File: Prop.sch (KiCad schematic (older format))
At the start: 11 parts

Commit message: some changes
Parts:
- added J? (x3): 1984989, PHOENIX_1984989, symbol 1984989:1984989
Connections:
- net labels added: +5V, MISO_1, MISO_2, MISO_3
- net labels removed: MISO, PWR
- wire segments 72 -> 64
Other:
- note added: "From Load Cell"
- note added: "From Pressure Transducer"
- note added: "From Thermocouple Connector"
- note added: "To Thermocouple"
- note removed: "Microcontroller"
- note removed: "Thermocouple"
- moved on the sheet: J?, Resistor, Resistor?, U?

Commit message: smaller capacitors
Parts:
- removed C? (x3): 0.1uF, symbol pspice:CAP
- added C (x3): 0.1 uF, symbol Device:C
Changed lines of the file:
@@
 Alumel_Lead
 Connection ~ 7300 2300
-Wire Wire Line
-	7300 2200 7300 2300
-Wire Wire Line
-	7300 1400 7300 1700
-$Comp
-L pspice:CAP C?
-U 1 1 603AE0E4
-P 7300 1950
-F 0 "C?" H 7478 1996 50  0000 L CNN
-F 1 "0.1uF" H 7478 1905 50  0000 L CNN
-F 2 "" H 7300 1950 50  0001 C CNN
-F 3 "~" H 7300 1950 50  0001 C CNN
-	1    7300 1950
-	1    0    0    -1
-$EndComp
 $Comp
 L MAX6675ISA_:MAX6675ISA+ U?
@@
 Text Notes 2000 1900 0    50   ~ 0
 Pressure\nTransducer
-$Comp
-L pspice:CAP C?
-U 1 1 6041617D
-P 3150 1800
-F 0 "C?" H 3328 1846 50  0000 L CNN
-F 1 "0.1uF" H 3328 1755 50  0000 L CNN
-F 2 "" H 3150 1800 50  0001 C CNN
-F 3 "~" H 3150 1800 50  0001 C CNN
-	1    3150 1800
-	1    0    0    -1
-$EndComp
 Wire Wire Line
 	4800 1900 5050 1900
@@
 Wire Wire Line
 	1650 1550 1350 1550
-Wire Wire Line
-	2650 1350 3150 1350
 Wire Wire Line
 	2850 1550 2650 1550
@@
 	3150 1200 3150 1350
 Wire Wire Line
-	3150 2050 3150 2200
-Wire Wire Line
-	3150 2200 2850 2200
-Wire Wire Line
-	2850 2200 2850 1550
+	3150 1850 3150 2000
+Wire Wire Line
+	3150 2000 2850 2000
+Wire Wire Line
+	2850 2000 2850 1550
 $Comp
 L power:GND #PWR?
 U 1 1 603FE602
-P 3150 2350
-F 0 "#PWR?" H 3150 2100 50  0001 C CNN
-F 1 "GND" H 3155 2177 50  0000 C CNN
-F 2 "" H 3150 2350 50  0001 C CNN
-F 3 "" H 3150 2350 50  0001 C CNN
-	1    3150 2350
-	1    0    0    -1
-$EndComp
-Wire Wire Line
-	3150 2350 3150 2200
-Connection ~ 3150 2200
+P 3150 2150
+F 0 "#PWR?" H 3150 1900 50  0001 C CNN
+F 1 "GND" H 3155 1977 50  0000 C CNN
+F 2 "" H 3150 2150 50  0001 C CNN
+F 3 "" H 3150 2150 50  0001 C CNN
+	1    3150 2150
+	1    0    0    -1
+$EndComp
+Wire Wire Line
+	3150 2150 3150 2000
+Connection ~ 3150 2000
 Wire Wire Line
 	7300 1400 7300 1000
@@
 Wire Wire Line
 	4050 3850 4050 4750
-Wire Wire Line
-	2600 3400 2600 4050
 Connection ~ 1200 3400
 Wire Wire Line
@@
 	1    0    0    -1
 $EndComp
-$Comp
-L pspice:CAP C?
-U 1 1 60425283
-P 2600 4300
-F 0 "C?" H 2778 4346 50  0000 L CNN
-F 1 "0.1uF" H 2778 4255 50  0000 L CNN
-F 2 "" H 2600 4300 50  0001 C CNN
-F 3 "~" H 2600 4300 50  0001 C CNN
-	1    2600 4300
-	1    0    0    -1
-$EndComp
-Wire Wire Line
-	2600 4550 2600 4750
 $Comp
 L power:GND #PWR?
@@
 Text Notes 7450 3950 0    50   ~ 0
 From Pressure Transducer
+$Comp
+L Device:C C
+U 1 1 603C3DD0
+P 3150 1700
+F 0 "C" H 3265 1746 50  0000 L CNN
+F 1 "0.1 uF" H 3265 1655 50  0000 L CNN
+F 2 "" H 3188 1550 50  0001 C CNN
+F 3 "~" H 3150 1700 50  0001 C CNN
+	1    3150 1700
+	1    0    0    -1
+$EndComp
+Wire Wire Line
+	2650 1350 3150 1350
+$Comp
+L Device:C C
+U 1 1 603CA8F8
+P 7300 1950
+F 0 "C" H 7415 1996 50  0000 L CNN
+F 1 "0.1 uF" H 7415 1905 50  0000 L CNN
+F 2 "" H 7338 1800 50  0001 C CNN
+F 3 "~" H 7300 1950 50  0001 C CNN
+	1    7300 1950
+	1    0    0    -1
+$EndComp
+Wire Wire Line
+	7300 1400 7300 1800
+Wire Wire Line
+	7300 2100 7300 2300
+$Comp
+L Device:C C
+U 1 1 603D0090
+P 2600 4300
+F 0 "C" H 2715 4346 50  0000 L CNN
+F 1 "0.1 uF" H 2715 4255 50  0000 L CNN
+F 2 "" H 2638 4150 50  0001 C CNN
+F 3 "~" H 2600 4300 50  0001 C CNN
+	1    2600 4300
+	1    0    0    -1
+$EndComp
+Wire Wire Line
+	2600 3400 2600 4150
+Wire Wire Line
+	2600 4450 2600 4750
 $EndSCHEMATC

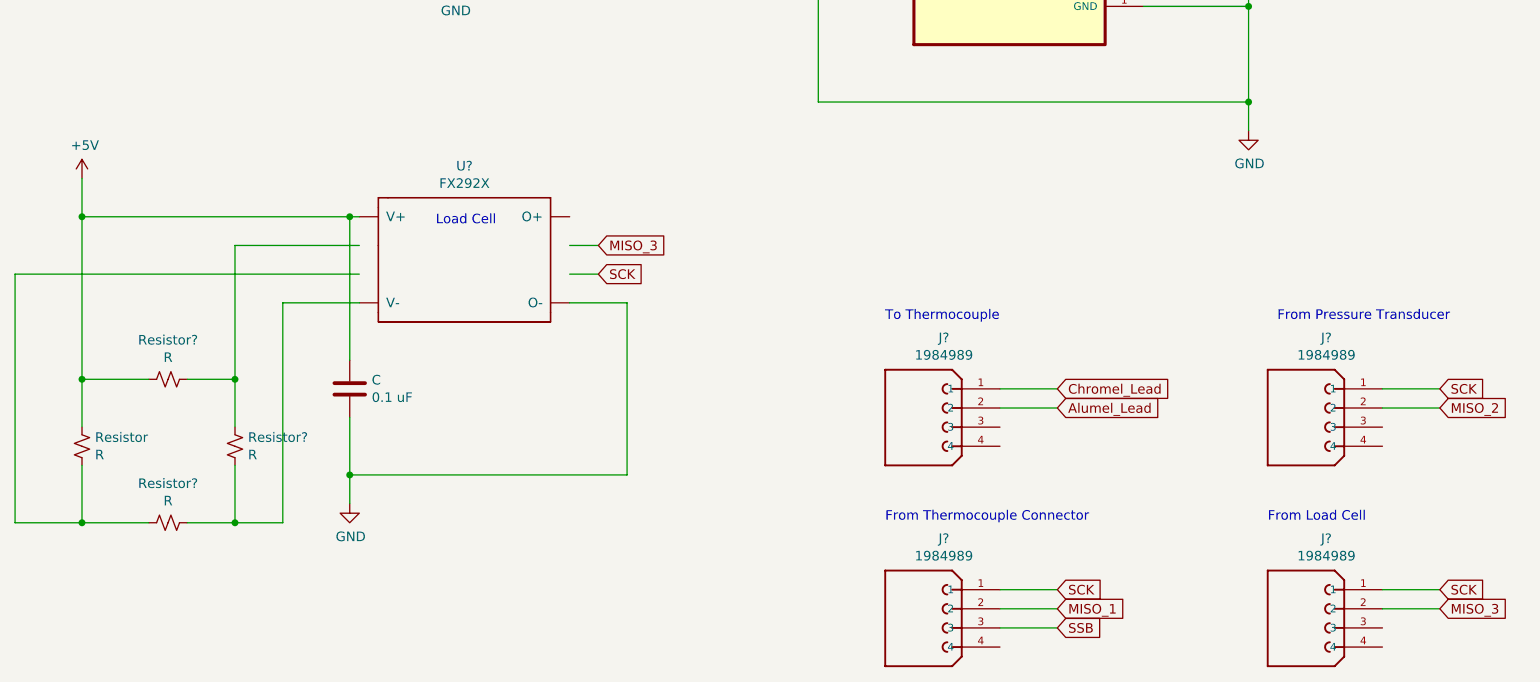
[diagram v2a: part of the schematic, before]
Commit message: changed load cell to have 4 pins
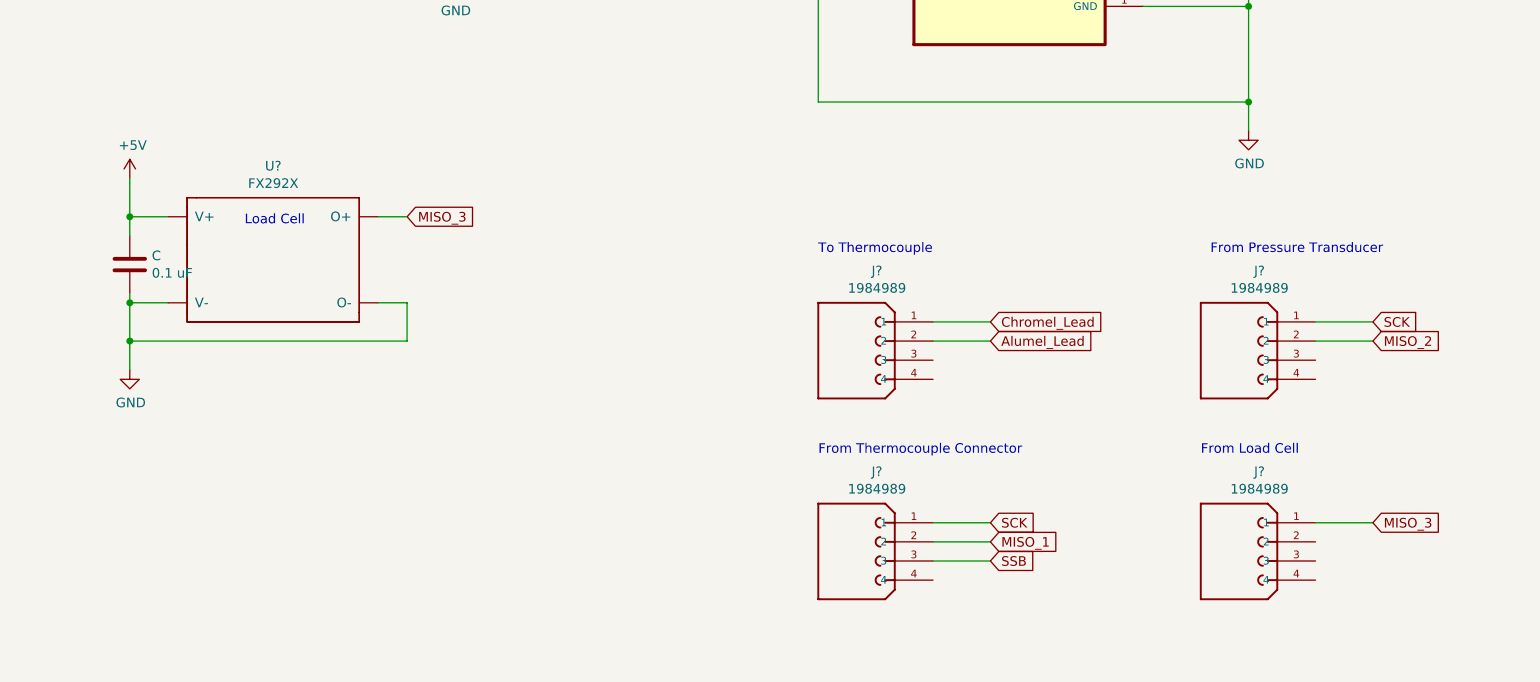
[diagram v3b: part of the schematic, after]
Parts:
- removed Resistor, Resistor? (x3): R, symbol Device:R_Small_US
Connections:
- wire segments 64 -> 46
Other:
- moved on the sheet: C, J?, U?

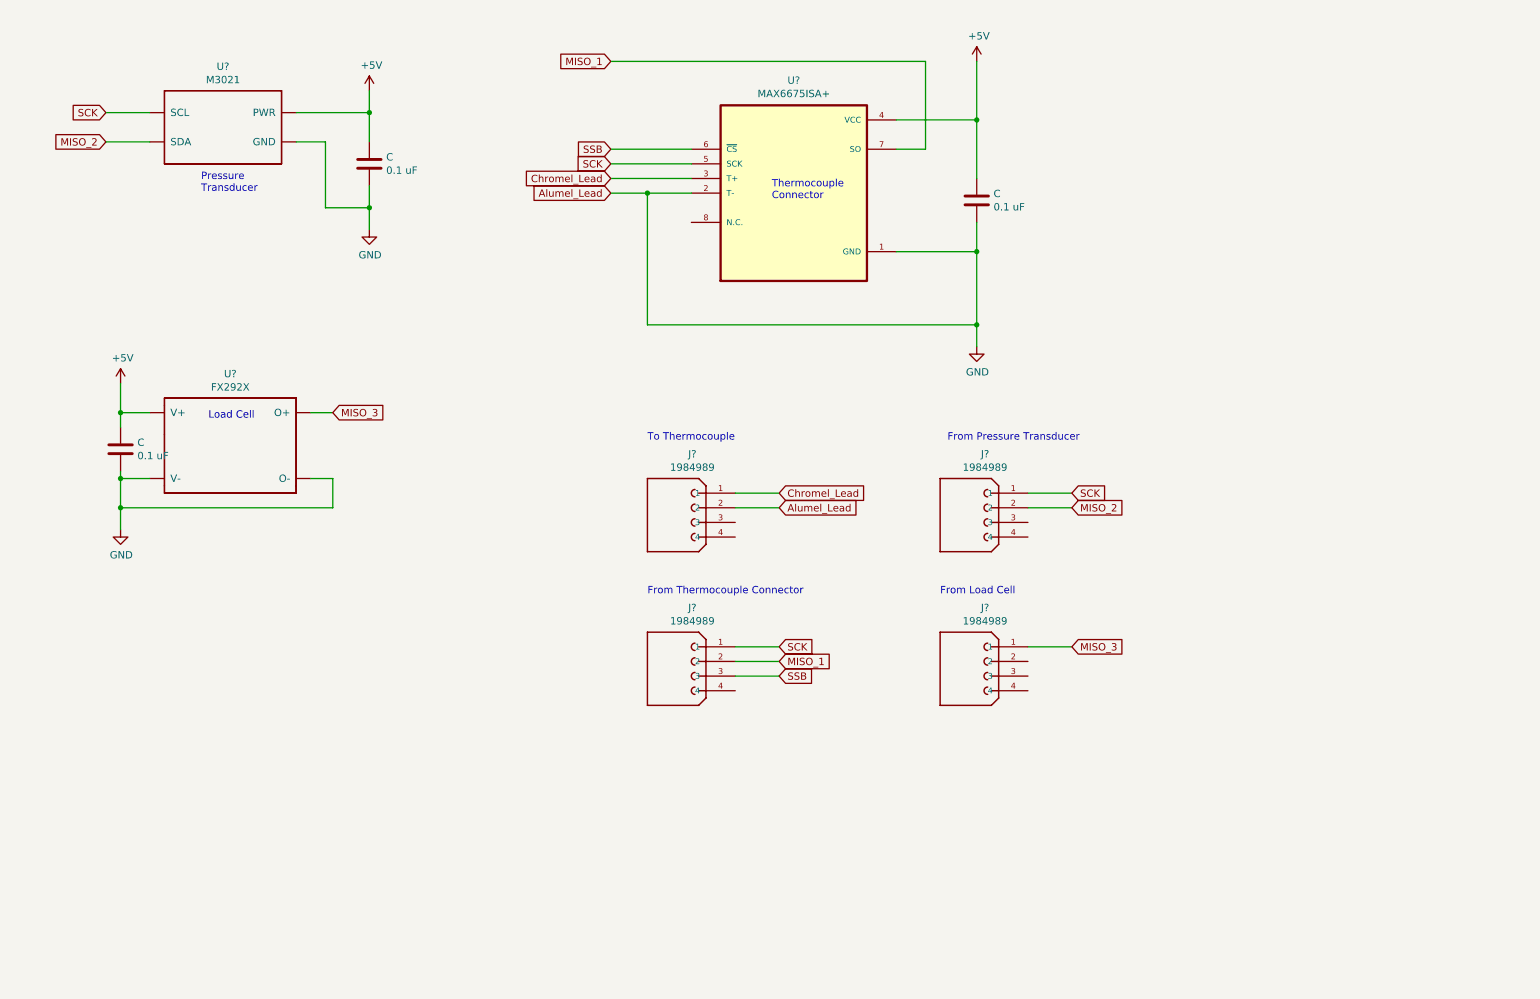
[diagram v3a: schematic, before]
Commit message: added ADC and amplifier
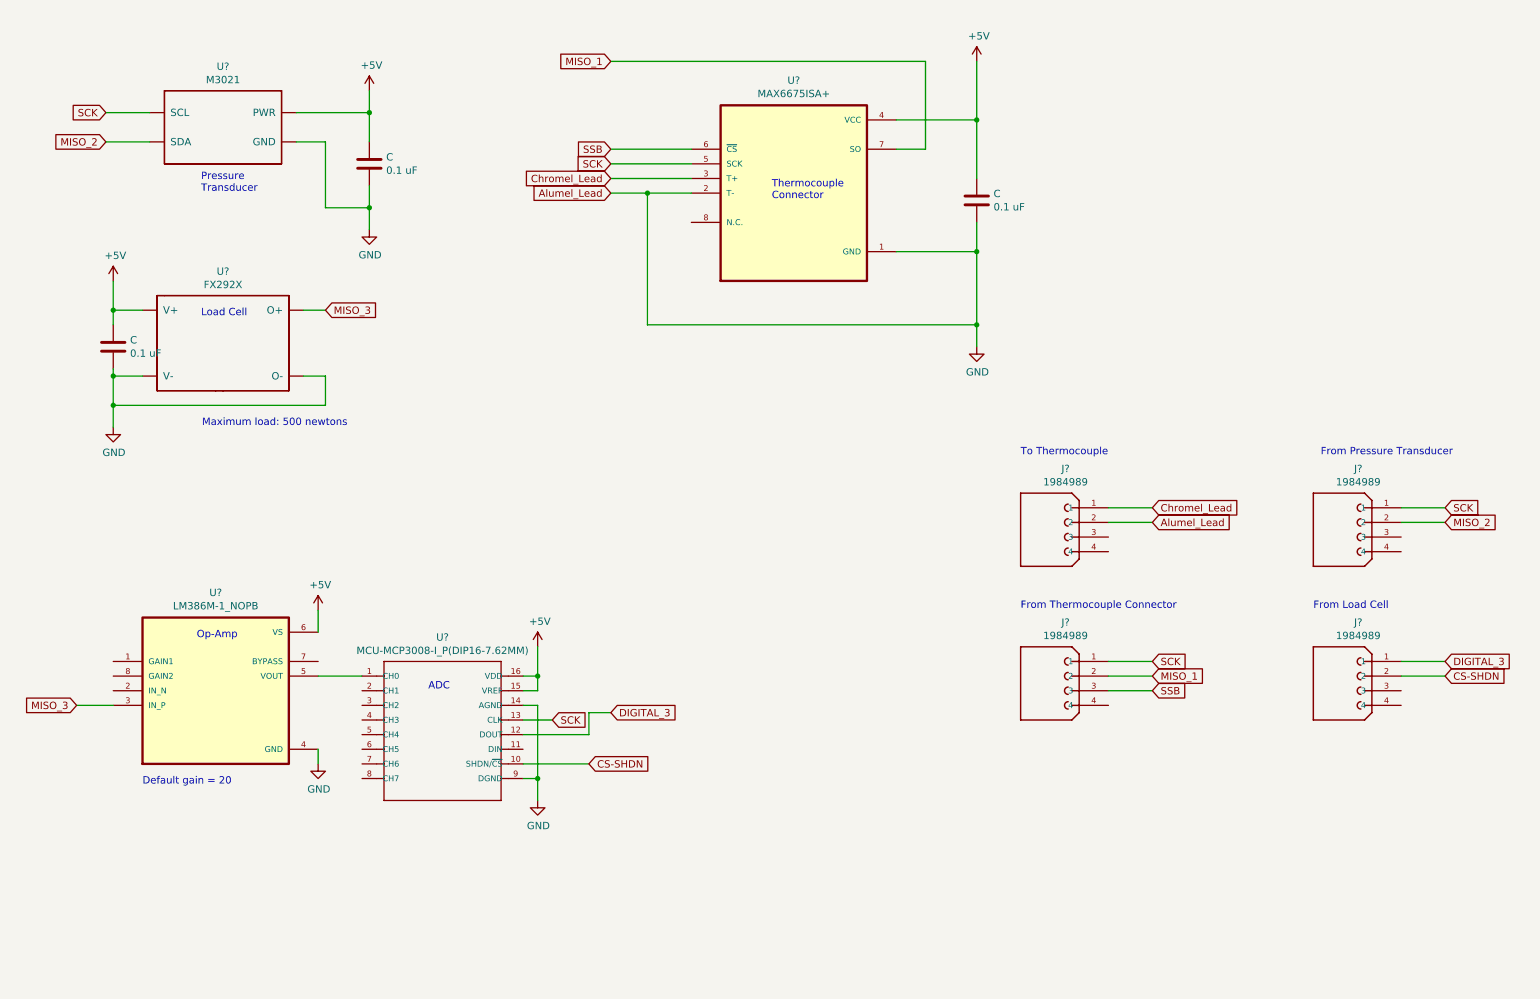
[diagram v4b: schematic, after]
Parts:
- added U?: MCU-MCP3008-I_P(DIP16-7.62MM), DIP16-2.54-19.2X7.62MM, symbol MCU-MCP3008-I_P_DIP16-7.62MM_:MCU-MCP3008-I_P(DIP16-7.62MM)
- added U?: LM386M-1_NOPB, SOIC127P599X175-8N, symbol LM386M-1_NOPB:LM386M-1_NOPB
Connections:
- net +5V: now also U?.15 (VREF), U?.16 (VDD), U?.6 (VS)
- net GND: now also U?.14 (AGND), U?.4 (GND), U?.9 (DGND)
- net MISO_3: now also U?.3 (IN_P); no longer J?.1
- net SCK: now also U?.13 (CLK)
- net CS-SHDN: now reaches J?.2
- net CS-SHDN: now also U?.10 (SHDN/~CS)
- new net: U?.1 (CH0), U?.5 (VOUT)
- new net DIGITAL_3: J?.1, U?.12 (DOUT)
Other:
- note added: "ADC"
- note added: "Default gain = 20"
- note added: "Maximum load: 500 newtons"
- note added: "Op-Amp"
- moved on the sheet: C, J?, U?

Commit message: updated amplifier, added hierarchical sheets
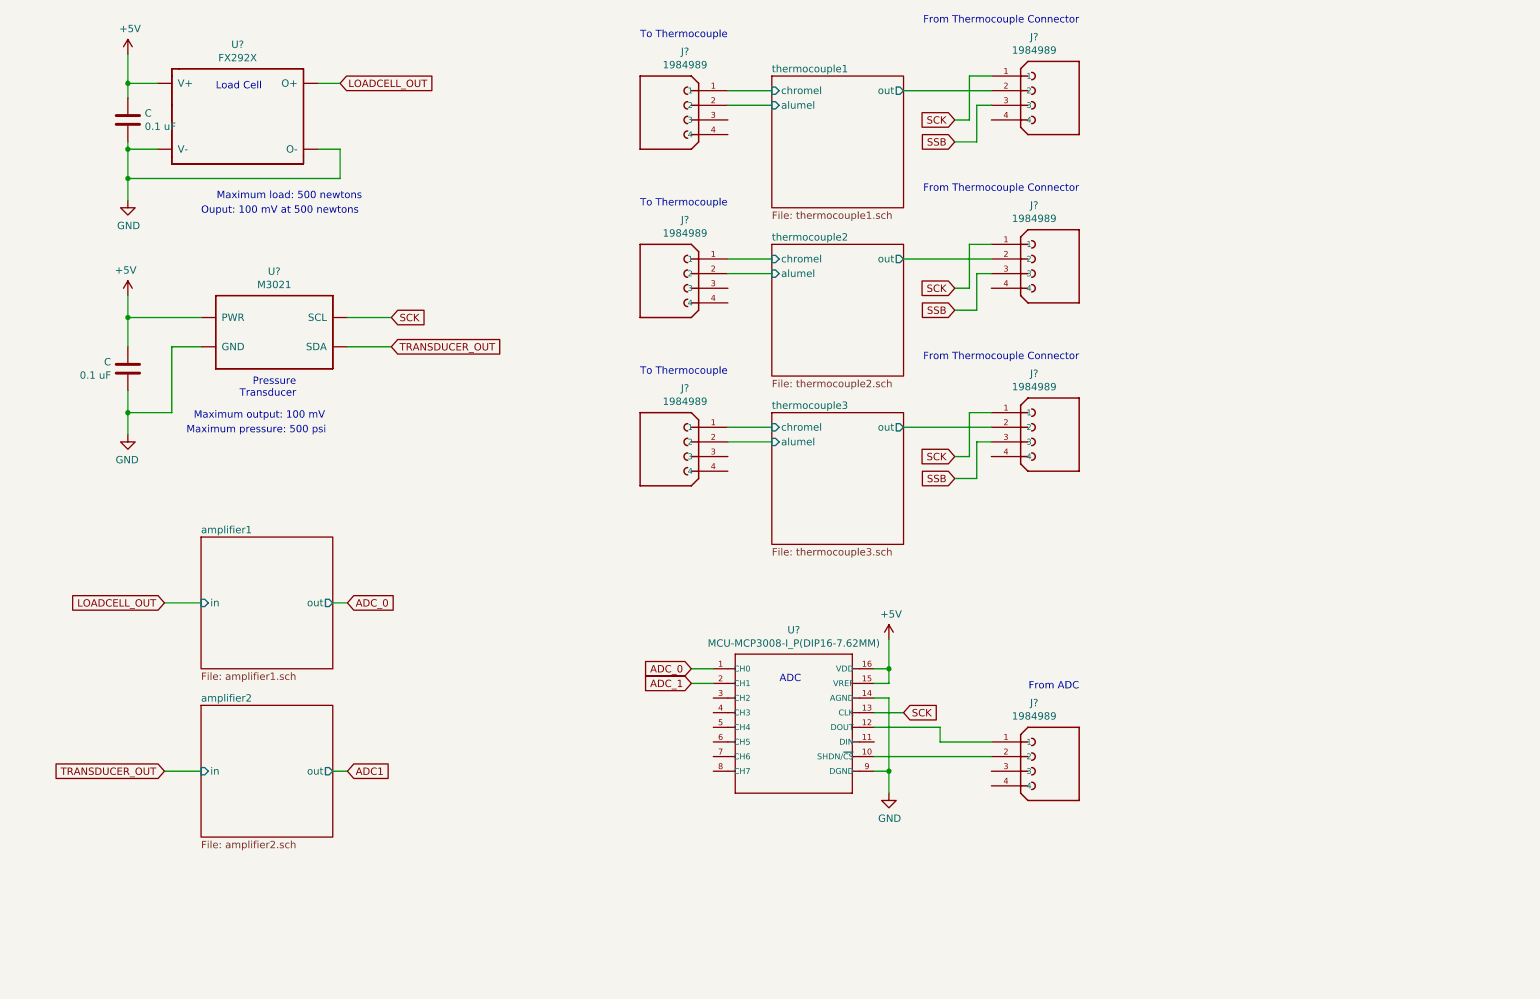
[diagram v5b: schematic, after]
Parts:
- removed C: 0.1 uF, symbol Device:C
- removed J?: 1984989, PHOENIX_1984989, symbol 1984989:1984989
- removed U?: MAX6675ISA+, SOIC127P600X175-8N, symbol MAX6675ISA_:MAX6675ISA+
- removed U?: LM386M-1_NOPB, SOIC127P599X175-8N, symbol LM386M-1_NOPB:LM386M-1_NOPB
- added J? (x4): 1984989, PHOENIX_1984989, symbol 1984989:1984989
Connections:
- net GND: no longer J?.2
- net SCK: now also J?.1, J?.1
- net SSB: now also J?.3, J?.3
- net ADC_0: now reaches U?.1 (CH0)
- net ADC_1: now reaches U?.2 (CH1)
- net CS-SHDN: no longer names the net of J?.2, U?.10 (SHDN/~CS)
- net Chromel_Lead renamed thermocouple1/chromel
- net DIGITAL_3: no longer names the net of J?.1, U?.12 (DOUT)
- net MISO_1 renamed thermocouple1/out
- net MISO_2 renamed TRANSDUCER_OUT
- net MISO_3 renamed LOADCELL_OUT
- new net thermocouple1/alumel: J?.2
- new net thermocouple2/alumel: J?.2
- new net thermocouple2/chromel: J?.1
- new net thermocouple2/out: J?.2
- new net thermocouple3/alumel: J?.2
- new net thermocouple3/chromel: J?.1
- new net thermocouple3/out: J?.2
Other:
- note added: "From ADC"
- note added: "Maximum output: 100 mV"
- note added: "Maximum pressure: 500 psi"
- note added: "Ouput: 100 mV at 500 newtons"
- note removed: "Default gain = 20"
- note removed: "From Load Cell"
- note removed: "From Pressure Transducer"
- note removed: "Op-Amp"
- note removed: "Thermocouple\nConnector"
- moved on the sheet: C, J?, U?
